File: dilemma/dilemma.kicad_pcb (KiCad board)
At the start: 2 copper layers, 154.5 x 108.7 mm, 91 parts, among them J1 S3B-PH-SM4-TB(LF)(SN), J2 Serial, J3 BATTERY_CONN_DEANS, J5 S3B-PH-SM4-TB(LF)(SN), SW1 SW_Push, SW10 SW_Push, SW11 SW_Push, SW12 SW_Push, SW13 SW_Push, SW14 SW_Push, SW15 SW_Push, SW16 SW_Push, SW17 locked, SW18 SW_Push, SW19 SW_Push, SW2 SW_Push, SW20 SW_Push, SW21 SW_Push, SW26 SW_SPST, SW3 SW_Push, SW37 SW_SPST, SW4 SW_Push, SW5 SW_Push, SW6 SW_Push, SW7 SW_Push, SW8 SW_Push, SW9 SW_Push, U2 eliteC

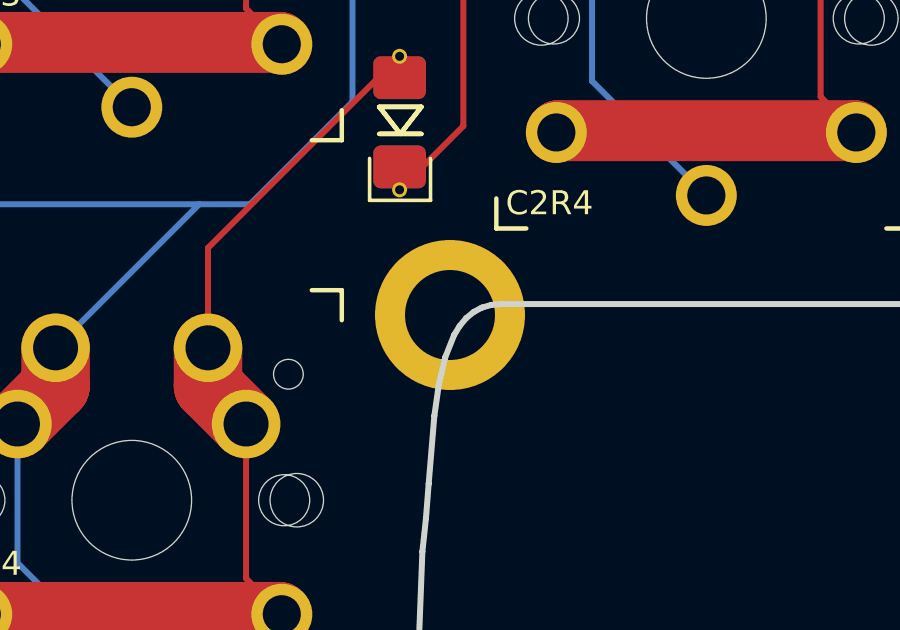
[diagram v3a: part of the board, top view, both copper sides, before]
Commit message: Remove H4 hole
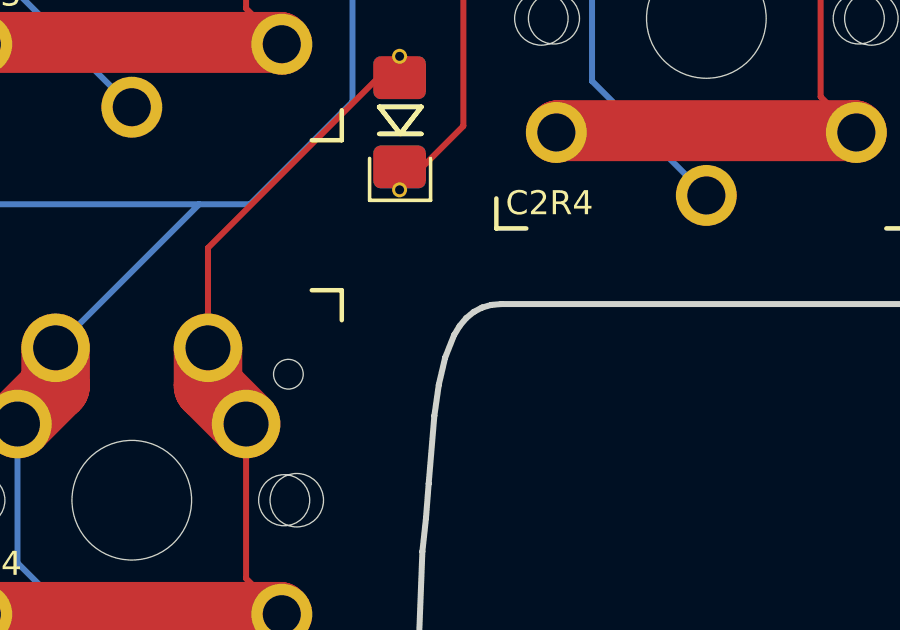
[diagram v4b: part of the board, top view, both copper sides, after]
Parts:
- removed H4: M4, local-libraries:MountingHole_3mm_Pad_thin
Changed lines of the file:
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@@
   (net 45 "Net-(D34-Pad2)")
   (net 46 "col6_l")
-  (net 47 "Net-(SW19-Pad2)")
-  (net 48 "Net-(SW20-Pad2)")
-  (net 49 "Net-(SW21-Pad2)")
+  (net 47 "Net-(D27-Pad2)")
+  (net 48 "Net-(D28-Pad2)")
+  (net 49 "Net-(D29-Pad2)")
   (footprint "local-libraries:MountingHole_3mm_Pad_thin" (layer "F.Cu")
     (at 236.12999 68.099328)
@@
       (net 5 "row4_l") (pinfunction "1") (pintype "passive"))
     (pad "2" thru_hole circle (at 2.54 -5.08) (size 2.286 2.286) (drill 1.4986) (layers *.Cu *.Mask)
-      (net 49 "Net-(SW21-Pad2)") (pinfunction "2") (pintype "passive"))
+      (net 49 "Net-(D29-Pad2)") (pinfunction "2") (pintype "passive"))
     (pad "2" thru_hole circle (at 3.81 -2.54) (size 2.286 2.286) (drill 1.4986) (layers *.Cu *.Mask)
-      (net 49 "Net-(SW21-Pad2)") (pinfunction "2") (pintype "passive"))
+      (net 49 "Net-(D29-Pad2)") (pinfunction "2") (pintype "passive"))
     (pad "2" thru_hole circle (at 5 3.8) (size 2.032 2.032) (drill 1.27) (layers *.Cu *.Mask)
-      (net 49 "Net-(SW21-Pad2)") (pinfunction "2") (pintype "passive"))
+      (net 49 "Net-(D29-Pad2)") (pinfunction "2") (pintype "passive"))
     (pad "2" thru_hole circle (at -5 3.8) (size 2.032 2.032) (drill 1.27) (layers *.Cu *.Mask)
-      (net 49 "Net-(SW21-Pad2)") (pinfunction "2") (pintype "passive"))
+      (net 49 "Net-(D29-Pad2)") (pinfunction "2") (pintype "passive"))
   )
   (footprint "local-libraries:kibuzzard-61F01C84" (layer "F.Cu")
@@
       (net 46 "col6_l") (pinfunction "K") (pintype "passive"))
     (pad "2" thru_hole circle (at 2.2 0 90) (size 0.5 0.5) (drill 0.3) (layers *.Cu *.Mask)
-      (net 47 "Net-(SW19-Pad2)") (pinfunction "A") (pintype "passive"))
+      (net 47 "Net-(D27-Pad2)") (pinfunction "A") (pintype "passive"))
     (pad "2" smd roundrect (at 1.4875 0 90) (size 1.425 1.75) (layers "B.Cu" "B.Paste" "B.Mask") (roundrect_rratio 0.175439)
-      (net 47 "Net-(SW19-Pad2)") (pinfunction "A") (pintype "passive"))
+      (net 47 "Net-(D27-Pad2)") (pinfunction "A") (pintype "passive"))
     (pad "2" smd roundrect (at 1.4875 0 90) (size 1.425 1.75) (layers "F.Cu" "F.Paste" "F.Mask") (roundrect_rratio 0.175439)
-      (net 47 "Net-(SW19-Pad2)") (pinfunction "A") (pintype "passive"))
+      (net 47 "Net-(D27-Pad2)") (pinfunction "A") (pintype "passive"))
   )
   (footprint "local-libraries:SW_MX_choc" (layer "F.Cu")
@@
       (net 1 "row2_l") (pinfunction "1") (pintype "passive"))
     (pad "2" thru_hole circle (at 3.81 -2.54) (size 2.286 2.286) (drill 1.4986) (layers *.Cu *.Mask)
-      (net 47 "Net-(SW19-Pad2)") (pinfunction "2") (pintype "passive"))
+      (net 47 "Net-(D27-Pad2)") (pinfunction "2") (pintype "passive"))
     (pad "2" thru_hole circle (at 5 3.8) (size 2.032 2.032) (drill 1.27) (layers *.Cu *.Mask)
-      (net 47 "Net-(SW19-Pad2)") (pinfunction "2") (pintype "passive"))
+      (net 47 "Net-(D27-Pad2)") (pinfunction "2") (pintype "passive"))
     (pad "2" thru_hole circle (at 2.54 -5.08) (size 2.286 2.286) (drill 1.4986) (layers *.Cu *.Mask)
-      (net 47 "Net-(SW19-Pad2)") (pinfunction "2") (pintype "passive"))
+      (net 47 "Net-(D27-Pad2)") (pinfunction "2") (pintype "passive"))
     (pad "2" thru_hole circle (at -5 3.8) (size 2.032 2.032) (drill 1.27) (layers *.Cu *.Mask)
-      (net 47 "Net-(SW19-Pad2)") (pinfunction "2") (pintype "passive"))
+      (net 47 "Net-(D27-Pad2)") (pinfunction "2") (pintype "passive"))
   )
   (footprint "local-libraries:SW_MX_choc" (layer "F.Cu")
@@
       (net 2 "Net-(D3-Pad2)") (pinfunction "2") (pintype "passive"))
   )
-  (footprint "local-libraries:MountingHole_3mm_Pad_thin" (layer "F.Cu")
-    (at 125.88 87.085)
-    (descr "Mounting Hole 3mm")
-    (tags "mounting hole 3mm")
-    (property "Sheetfile" "dilemma.kicad_sch")
-    (property "Sheetname" "")
-    (attr exclude_from_pos_files)
-    (fp_text reference "H4" (at 0 -4) (layer "F.SilkS") hide
-      (effects (font (size 1 1) (thickness 0.15)))
-    )
-    (fp_text value "M4" (at 0 4) (layer "F.Fab")
-      (effects (font (size 1 1) (thickness 0.15)))
-    )
-    (fp_text user "${REFERENCE}" (at 0 0) (layer "F.Fab")
-      (effects (font (size 1 1) (thickness 0.15)))
-    )
-    (fp_circle (center 0 0) (end 3 0) (layer "Cmts.User") (width 0.15) (fill none))
-    (fp_circle (center 0 0) (end 3.25 0) (layer "F.CrtYd") (width 0.05) (fill none))
-    (pad "1" thru_hole circle (at 0 0) (size 5 5) (drill 3) (layers *.Cu *.Mask)
-      (net 23 "Gnd_l") (pinfunction "1") (pintype "input"))
-  )
   (footprint "local-libraries:kibuzzard-628E0199" (layer "F.Cu")
     (at 214.325992 69.495 90)
@@
       (net 3 "row3_l") (pinfunction "1") (pintype "passive"))
     (pad "2" thru_hole circle (at 3.81 -2.54) (size 2.286 2.286) (drill 1.4986) (layers *.Cu *.Mask)
-      (net 48 "Net-(SW20-Pad2)") (pinfunction "2") (pintype "passive"))
+      (net 48 "Net-(D28-Pad2)") (pinfunction "2") (pintype "passive"))
     (pad "2" thru_hole circle (at 2.54 -5.08) (size 2.286 2.286) (drill 1.4986) (layers *.Cu *.Mask)
-      (net 48 "Net-(SW20-Pad2)") (pinfunction "2") (pintype "passive"))
+      (net 48 "Net-(D28-Pad2)") (pinfunction "2") (pintype "passive"))
     (pad "2" thru_hole circle (at -5 3.8) (size 2.032 2.032) (drill 1.27) (layers *.Cu *.Mask)
-      (net 48 "Net-(SW20-Pad2)") (pinfunction "2") (pintype "passive"))
+      (net 48 "Net-(D28-Pad2)") (pinfunction "2") (pintype "passive"))
     (pad "2" thru_hole circle (at 5 3.8) (size 2.032 2.032) (drill 1.27) (layers *.Cu *.Mask)
-      (net 48 "Net-(SW20-Pad2)") (pinfunction "2") (pintype "passive"))
+      (net 48 "Net-(D28-Pad2)") (pinfunction "2") (pintype "passive"))
   )
   (footprint "local-libraries:D_1206_handsolder_reversible" (layer "F.Cu")
@@
       (net 46 "col6_l") (pinfunction "K") (pintype "passive"))
     (pad "2" thru_hole circle (at 2.2 0 90) (size 0.5 0.5) (drill 0.3) (layers *.Cu *.Mask)
-      (net 48 "Net-(SW20-Pad2)") (pinfunction "A") (pintype "passive"))
+      (net 48 "Net-(D28-Pad2)") (pinfunction "A") (pintype "passive"))
     (pad "2" smd roundrect (at 1.4875 0 90) (size 1.425 1.75) (layers "F.Cu" "F.Paste" "F.Mask") (roundrect_rratio 0.175439)
-      (net 48 "Net-(SW20-Pad2)") (pinfunction "A") (pintype "passive"))
+      (net 48 "Net-(D28-Pad2)") (pinfunction "A") (pintype "passive"))
     (pad "2" smd roundrect (at 1.4875 0 90) (size 1.425 1.75) (layers "B.Cu" "B.Paste" "B.Mask") (roundrect_rratio 0.175439)
-      (net 48 "Net-(SW20-Pad2)") (pinfunction "A") (pintype "passive"))
+      (net 48 "Net-(D28-Pad2)") (pinfunction "A") (pintype "passive"))
   )
   (footprint "local-libraries:D_1206_handsolder_reversible" (layer "F.Cu")
@@
       (net 46 "col6_l") (pinfunction "K") (pintype "passive"))
     (pad "2" smd roundrect (at 1.4875 0 90) (size 1.425 1.75) (layers "B.Cu" "B.Paste" "B.Mask") (roundrect_rratio 0.175439)
-      (net 49 "Net-(SW21-Pad2)") (pinfunction "A") (pintype "passive"))
+      (net 49 "Net-(D29-Pad2)") (pinfunction "A") (pintype "passive"))
     (pad "2" smd roundrect (at 1.4875 0 90) (size 1.425 1.75) (layers "F.Cu" "F.Paste" "F.Mask") (roundrect_rratio 0.175439)
-      (net 49 "Net-(SW21-Pad2)") (pinfunction "A") (pintype "passive"))
+      (net 49 "Net-(D29-Pad2)") (pinfunction "A") (pintype "passive"))
     (pad "2" thru_hole circle (at 2.2 0 90) (size 0.5 0.5) (drill 0.3) (layers *.Cu *.Mask)
-      (net 49 "Net-(SW21-Pad2)") (pinfunction "A") (pintype "passive"))
+      (net 49 "Net-(D29-Pad2)") (pinfunction "A") (pintype "passive"))
   )
   (footprint "local-libraries:Switch_MSK-12C01-07" (layer "F.Cu")
@@
   (segment (start 222.398471 71.026529) (end 222.24 71.185) (width 0.4) (layer "B.Cu") (net 41))
   (segment (start 223.937 80.518) (end 222.25 80.518) (width 0.2) (layer "F.Cu") (net 42))
-  (segment (start 224.81 79.295) (end 224.81 79.645) (width 0.2) (layer "F.Cu") (net 42))
   (segment (start 224.81 79.645) (end 223.937 80.518) (width 0.2) (layer "F.Cu") (net 42))
+  (segment (start 224.81 79.295) (end 224.81 79.645) (width 0.2) (layer "F.Cu") (net 42))
   (via (at 222.25 80.518) (size 0.5) (drill 0.3) (layers "F.Cu" "B.Cu") (net 42))
   (segment (start 221.613 80.518) (end 220.39 79.295) (width 0.2) (layer "B.Cu") (net 42))

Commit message: Revert "Remove H4 hole"
This reverts commit eafe3389c8530ed03ec8ad130b3a2f53ccdd09a2.
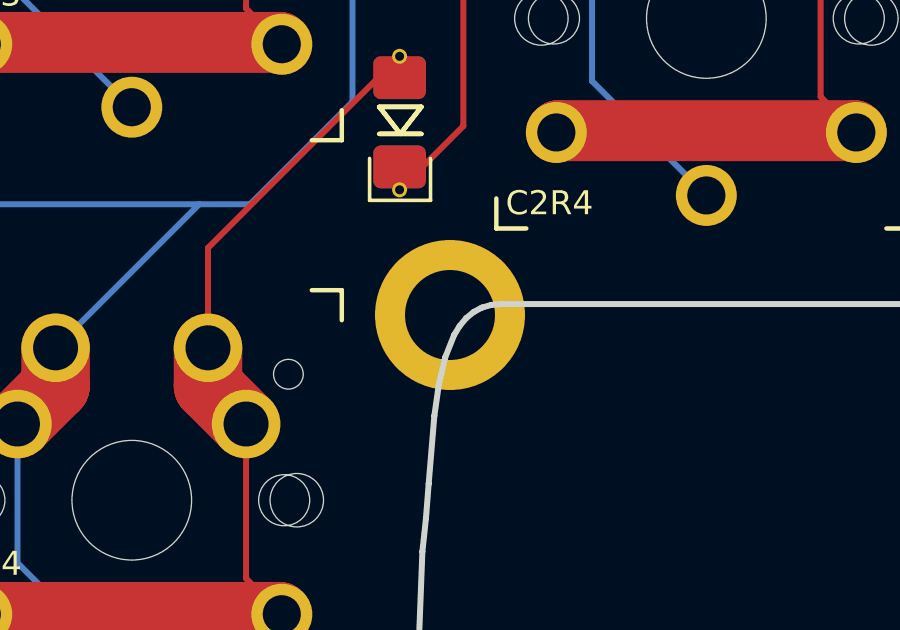
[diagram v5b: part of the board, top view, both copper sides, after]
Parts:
- added H4: M4, local-libraries:MountingHole_3mm_Pad_thin, F.Cu at (125.9, 87.1)
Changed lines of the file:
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@@
   (net 45 "Net-(D34-Pad2)")
   (net 46 "col6_l")
-  (net 47 "Net-(D27-Pad2)")
-  (net 48 "Net-(D28-Pad2)")
-  (net 49 "Net-(D29-Pad2)")
+  (net 47 "Net-(SW19-Pad2)")
+  (net 48 "Net-(SW20-Pad2)")
+  (net 49 "Net-(SW21-Pad2)")
   (footprint "local-libraries:MountingHole_3mm_Pad_thin" (layer "F.Cu")
     (at 236.12999 68.099328)
@@
       (net 5 "row4_l") (pinfunction "1") (pintype "passive"))
     (pad "2" thru_hole circle (at 2.54 -5.08) (size 2.286 2.286) (drill 1.4986) (layers *.Cu *.Mask)
-      (net 49 "Net-(D29-Pad2)") (pinfunction "2") (pintype "passive"))
+      (net 49 "Net-(SW21-Pad2)") (pinfunction "2") (pintype "passive"))
     (pad "2" thru_hole circle (at 3.81 -2.54) (size 2.286 2.286) (drill 1.4986) (layers *.Cu *.Mask)
-      (net 49 "Net-(D29-Pad2)") (pinfunction "2") (pintype "passive"))
+      (net 49 "Net-(SW21-Pad2)") (pinfunction "2") (pintype "passive"))
     (pad "2" thru_hole circle (at 5 3.8) (size 2.032 2.032) (drill 1.27) (layers *.Cu *.Mask)
-      (net 49 "Net-(D29-Pad2)") (pinfunction "2") (pintype "passive"))
+      (net 49 "Net-(SW21-Pad2)") (pinfunction "2") (pintype "passive"))
     (pad "2" thru_hole circle (at -5 3.8) (size 2.032 2.032) (drill 1.27) (layers *.Cu *.Mask)
-      (net 49 "Net-(D29-Pad2)") (pinfunction "2") (pintype "passive"))
+      (net 49 "Net-(SW21-Pad2)") (pinfunction "2") (pintype "passive"))
   )
   (footprint "local-libraries:kibuzzard-61F01C84" (layer "F.Cu")
@@
       (net 46 "col6_l") (pinfunction "K") (pintype "passive"))
     (pad "2" thru_hole circle (at 2.2 0 90) (size 0.5 0.5) (drill 0.3) (layers *.Cu *.Mask)
-      (net 47 "Net-(D27-Pad2)") (pinfunction "A") (pintype "passive"))
+      (net 47 "Net-(SW19-Pad2)") (pinfunction "A") (pintype "passive"))
     (pad "2" smd roundrect (at 1.4875 0 90) (size 1.425 1.75) (layers "B.Cu" "B.Paste" "B.Mask") (roundrect_rratio 0.175439)
-      (net 47 "Net-(D27-Pad2)") (pinfunction "A") (pintype "passive"))
+      (net 47 "Net-(SW19-Pad2)") (pinfunction "A") (pintype "passive"))
     (pad "2" smd roundrect (at 1.4875 0 90) (size 1.425 1.75) (layers "F.Cu" "F.Paste" "F.Mask") (roundrect_rratio 0.175439)
-      (net 47 "Net-(D27-Pad2)") (pinfunction "A") (pintype "passive"))
+      (net 47 "Net-(SW19-Pad2)") (pinfunction "A") (pintype "passive"))
   )
   (footprint "local-libraries:SW_MX_choc" (layer "F.Cu")
@@
       (net 1 "row2_l") (pinfunction "1") (pintype "passive"))
     (pad "2" thru_hole circle (at 3.81 -2.54) (size 2.286 2.286) (drill 1.4986) (layers *.Cu *.Mask)
-      (net 47 "Net-(D27-Pad2)") (pinfunction "2") (pintype "passive"))
+      (net 47 "Net-(SW19-Pad2)") (pinfunction "2") (pintype "passive"))
     (pad "2" thru_hole circle (at 5 3.8) (size 2.032 2.032) (drill 1.27) (layers *.Cu *.Mask)
-      (net 47 "Net-(D27-Pad2)") (pinfunction "2") (pintype "passive"))
+      (net 47 "Net-(SW19-Pad2)") (pinfunction "2") (pintype "passive"))
     (pad "2" thru_hole circle (at 2.54 -5.08) (size 2.286 2.286) (drill 1.4986) (layers *.Cu *.Mask)
-      (net 47 "Net-(D27-Pad2)") (pinfunction "2") (pintype "passive"))
+      (net 47 "Net-(SW19-Pad2)") (pinfunction "2") (pintype "passive"))
     (pad "2" thru_hole circle (at -5 3.8) (size 2.032 2.032) (drill 1.27) (layers *.Cu *.Mask)
-      (net 47 "Net-(D27-Pad2)") (pinfunction "2") (pintype "passive"))
+      (net 47 "Net-(SW19-Pad2)") (pinfunction "2") (pintype "passive"))
   )
   (footprint "local-libraries:SW_MX_choc" (layer "F.Cu")
@@
       (net 2 "Net-(D3-Pad2)") (pinfunction "2") (pintype "passive"))
   )
+  (footprint "local-libraries:MountingHole_3mm_Pad_thin" (layer "F.Cu")
+    (at 125.88 87.085)
+    (descr "Mounting Hole 3mm")
+    (tags "mounting hole 3mm")
+    (property "Sheetfile" "dilemma.kicad_sch")
+    (property "Sheetname" "")
+    (attr exclude_from_pos_files)
+    (fp_text reference "H4" (at 0 -4) (layer "F.SilkS") hide
+      (effects (font (size 1 1) (thickness 0.15)))
+    )
+    (fp_text value "M4" (at 0 4) (layer "F.Fab")
+      (effects (font (size 1 1) (thickness 0.15)))
+    )
+    (fp_text user "${REFERENCE}" (at 0 0) (layer "F.Fab")
+      (effects (font (size 1 1) (thickness 0.15)))
+    )
+    (fp_circle (center 0 0) (end 3 0) (layer "Cmts.User") (width 0.15) (fill none))
+    (fp_circle (center 0 0) (end 3.25 0) (layer "F.CrtYd") (width 0.05) (fill none))
+    (pad "1" thru_hole circle (at 0 0) (size 5 5) (drill 3) (layers *.Cu *.Mask)
+      (net 23 "Gnd_l") (pinfunction "1") (pintype "input"))
+  )
   (footprint "local-libraries:kibuzzard-628E0199" (layer "F.Cu")
     (at 214.325992 69.495 90)
@@
       (net 3 "row3_l") (pinfunction "1") (pintype "passive"))
     (pad "2" thru_hole circle (at 3.81 -2.54) (size 2.286 2.286) (drill 1.4986) (layers *.Cu *.Mask)
-      (net 48 "Net-(D28-Pad2)") (pinfunction "2") (pintype "passive"))
+      (net 48 "Net-(SW20-Pad2)") (pinfunction "2") (pintype "passive"))
     (pad "2" thru_hole circle (at 2.54 -5.08) (size 2.286 2.286) (drill 1.4986) (layers *.Cu *.Mask)
-      (net 48 "Net-(D28-Pad2)") (pinfunction "2") (pintype "passive"))
+      (net 48 "Net-(SW20-Pad2)") (pinfunction "2") (pintype "passive"))
     (pad "2" thru_hole circle (at -5 3.8) (size 2.032 2.032) (drill 1.27) (layers *.Cu *.Mask)
-      (net 48 "Net-(D28-Pad2)") (pinfunction "2") (pintype "passive"))
+      (net 48 "Net-(SW20-Pad2)") (pinfunction "2") (pintype "passive"))
     (pad "2" thru_hole circle (at 5 3.8) (size 2.032 2.032) (drill 1.27) (layers *.Cu *.Mask)
-      (net 48 "Net-(D28-Pad2)") (pinfunction "2") (pintype "passive"))
+      (net 48 "Net-(SW20-Pad2)") (pinfunction "2") (pintype "passive"))
   )
   (footprint "local-libraries:D_1206_handsolder_reversible" (layer "F.Cu")
@@
       (net 46 "col6_l") (pinfunction "K") (pintype "passive"))
     (pad "2" thru_hole circle (at 2.2 0 90) (size 0.5 0.5) (drill 0.3) (layers *.Cu *.Mask)
-      (net 48 "Net-(D28-Pad2)") (pinfunction "A") (pintype "passive"))
+      (net 48 "Net-(SW20-Pad2)") (pinfunction "A") (pintype "passive"))
     (pad "2" smd roundrect (at 1.4875 0 90) (size 1.425 1.75) (layers "F.Cu" "F.Paste" "F.Mask") (roundrect_rratio 0.175439)
-      (net 48 "Net-(D28-Pad2)") (pinfunction "A") (pintype "passive"))
+      (net 48 "Net-(SW20-Pad2)") (pinfunction "A") (pintype "passive"))
     (pad "2" smd roundrect (at 1.4875 0 90) (size 1.425 1.75) (layers "B.Cu" "B.Paste" "B.Mask") (roundrect_rratio 0.175439)
-      (net 48 "Net-(D28-Pad2)") (pinfunction "A") (pintype "passive"))
+      (net 48 "Net-(SW20-Pad2)") (pinfunction "A") (pintype "passive"))
   )
   (footprint "local-libraries:D_1206_handsolder_reversible" (layer "F.Cu")
@@
       (net 46 "col6_l") (pinfunction "K") (pintype "passive"))
     (pad "2" smd roundrect (at 1.4875 0 90) (size 1.425 1.75) (layers "B.Cu" "B.Paste" "B.Mask") (roundrect_rratio 0.175439)
-      (net 49 "Net-(D29-Pad2)") (pinfunction "A") (pintype "passive"))
+      (net 49 "Net-(SW21-Pad2)") (pinfunction "A") (pintype "passive"))
     (pad "2" smd roundrect (at 1.4875 0 90) (size 1.425 1.75) (layers "F.Cu" "F.Paste" "F.Mask") (roundrect_rratio 0.175439)
-      (net 49 "Net-(D29-Pad2)") (pinfunction "A") (pintype "passive"))
+      (net 49 "Net-(SW21-Pad2)") (pinfunction "A") (pintype "passive"))
     (pad "2" thru_hole circle (at 2.2 0 90) (size 0.5 0.5) (drill 0.3) (layers *.Cu *.Mask)
-      (net 49 "Net-(D29-Pad2)") (pinfunction "A") (pintype "passive"))
+      (net 49 "Net-(SW21-Pad2)") (pinfunction "A") (pintype "passive"))
   )
   (footprint "local-libraries:Switch_MSK-12C01-07" (layer "F.Cu")
@@
   (segment (start 222.398471 71.026529) (end 222.24 71.185) (width 0.4) (layer "B.Cu") (net 41))
   (segment (start 223.937 80.518) (end 222.25 80.518) (width 0.2) (layer "F.Cu") (net 42))
-  (segment (start 224.81 79.645) (end 223.937 80.518) (width 0.2) (layer "F.Cu") (net 42))
   (segment (start 224.81 79.295) (end 224.81 79.645) (width 0.2) (layer "F.Cu") (net 42))
+  (segment (start 224.81 79.645) (end 223.937 80.518) (width 0.2) (layer "F.Cu") (net 42))
   (via (at 222.25 80.518) (size 0.5) (drill 0.3) (layers "F.Cu" "B.Cu") (net 42))
   (segment (start 221.613 80.518) (end 220.39 79.295) (width 0.2) (layer "B.Cu") (net 42))
